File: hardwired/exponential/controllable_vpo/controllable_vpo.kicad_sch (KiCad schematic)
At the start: 16 parts, among them Q1 NPN, Q2 NPN, U1 ${SIM.PARAMS}, U2 ${SIM.PARAMS}, U3 ${SIM.PARAMS}

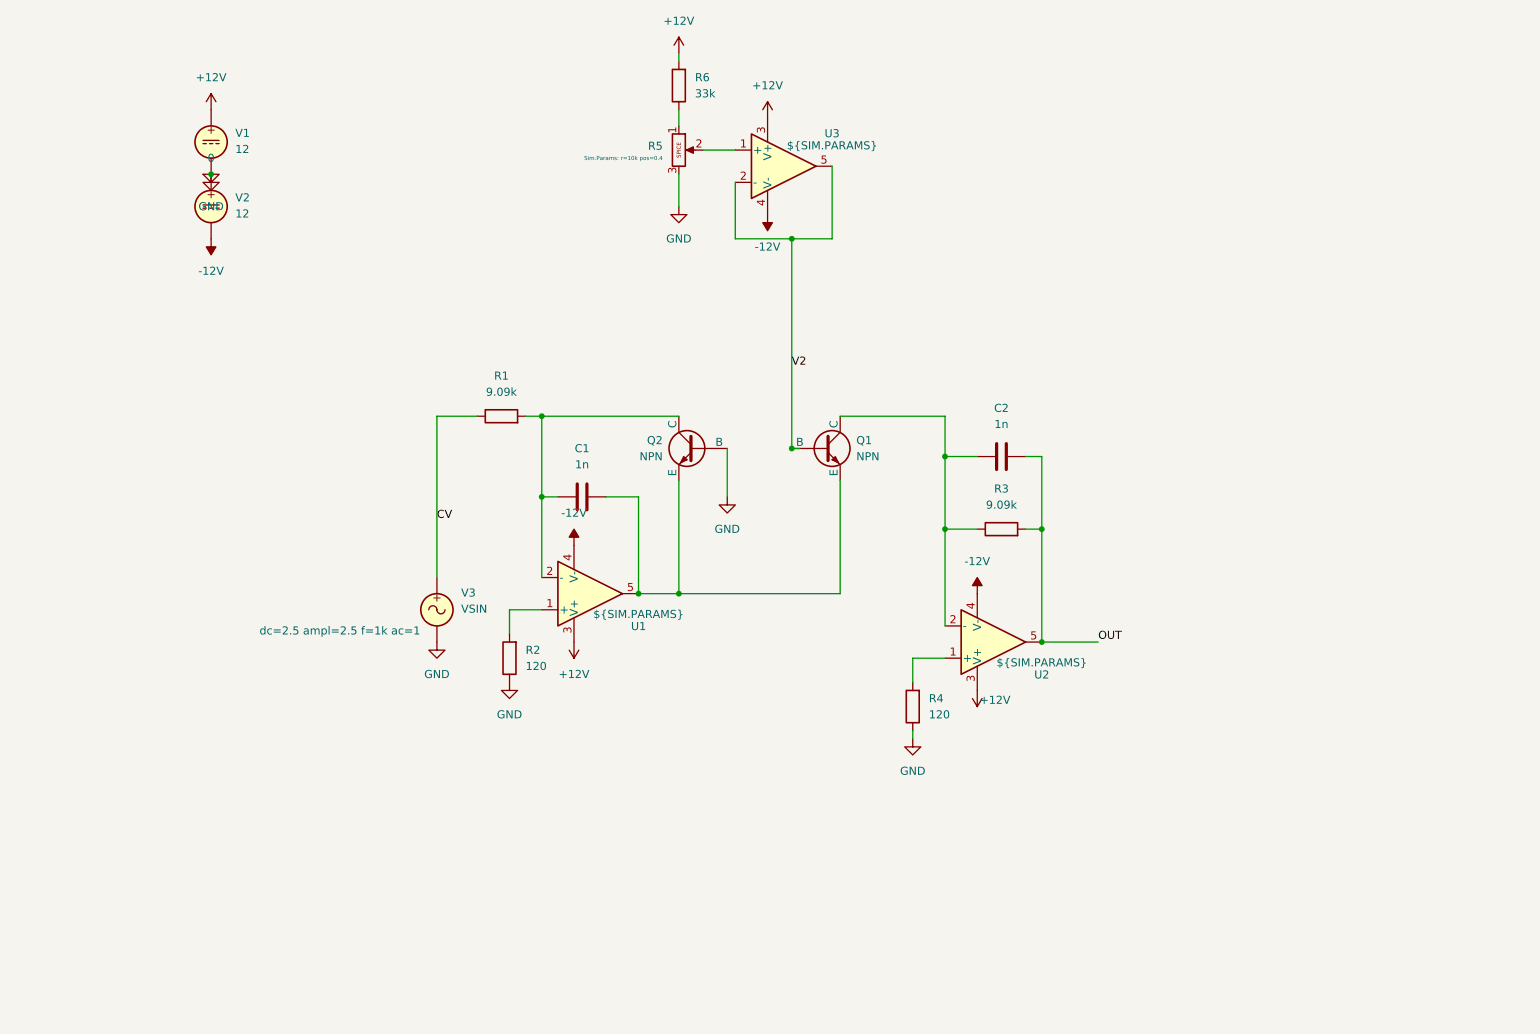
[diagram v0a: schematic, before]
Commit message: Add new Volt Per Octave circuit.  Thank you Copilot!
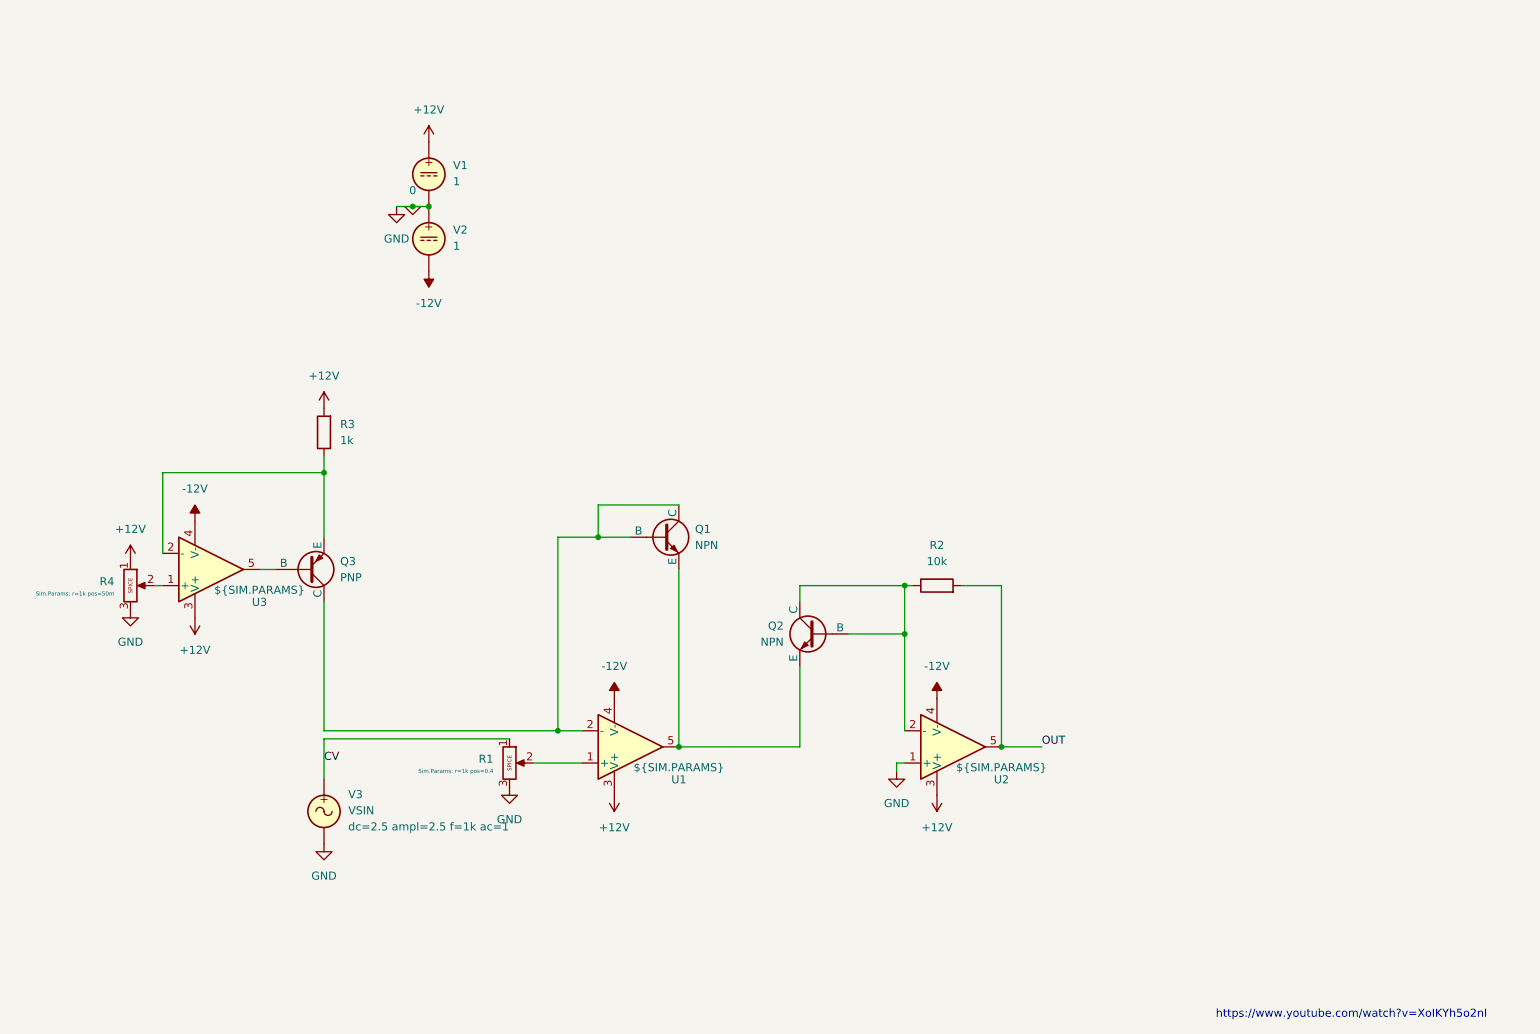
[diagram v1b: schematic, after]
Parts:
- removed C1, C2: 1n, symbol Device:C
- removed R1: 9.09k, symbol Device:R
- removed R4: 120, symbol Device:R
- removed R5: Potentiometer, symbol Simulation_SPICE:Potentiometer
- removed R6: 33k, symbol Device:R
- added Q3: PNP, symbol Simulation_SPICE:PNP
- added R1, R4: Potentiometer, symbol Simulation_SPICE:Potentiometer
- R2: value 120 -> 10k
- R3: value 9.09k -> 1k
- V1, V2: value 12 -> 1
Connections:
- net +12V: now also R3.2, R4.1
- net 0: now also U2.1 (+), R1.3, R4.3; no longer Q2.2 (B), R2.1
- net CV: now also R1.1
- net OUT: now also R2.2; no longer R3.2
- net at U3.1 (+): now also R4.2
- net at Q2.1 (C): now also Q2.2 (B), R2.1, U2.2 (-); no longer U1.2 (-)
- net at U1.1 (+): now also R1.2; no longer R2.2
- removed net V2: Q1.2 (B), U3.2 (-), U3.5
- new net: Q1.1 (C), Q1.2 (B), Q3.1 (C), U1.2 (-)
- new net: Q3.2 (B), U3.5
- new net: Q3.3 (E), R3.1, U3.2 (-)
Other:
- note added: "https://www.youtube.com/watch?v=XoIKYh5o2nI"
